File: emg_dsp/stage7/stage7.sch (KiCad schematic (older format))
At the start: 202 parts, among them U1 RS232_CON, U10 EN_VDD, U11 USBLC6, U12 ABM10XTAL-24, U13 BF527, U14 MIC5365, U15 AT25DF041-MHF, U16 ADSP_JTAG_CON, U17 LAN8710A, U18 74LCX541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

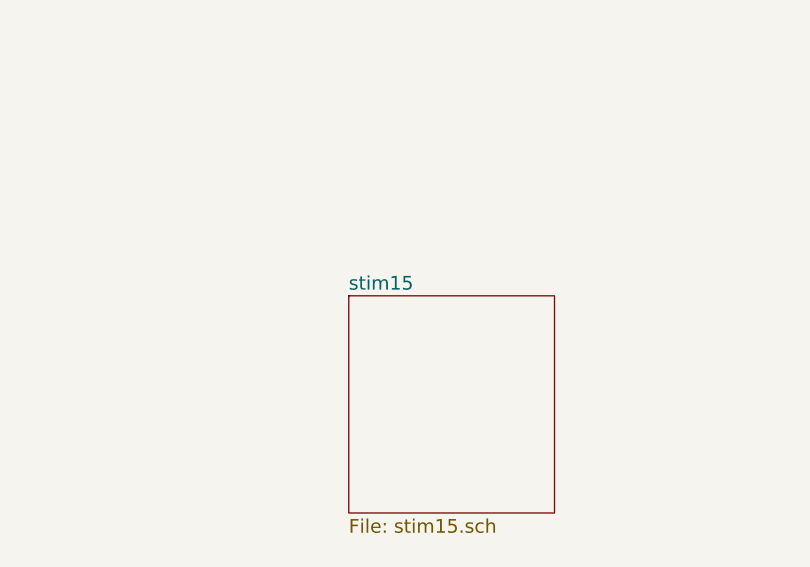
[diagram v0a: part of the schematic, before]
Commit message: placed modules in stim and wired, issues with shorting in stims
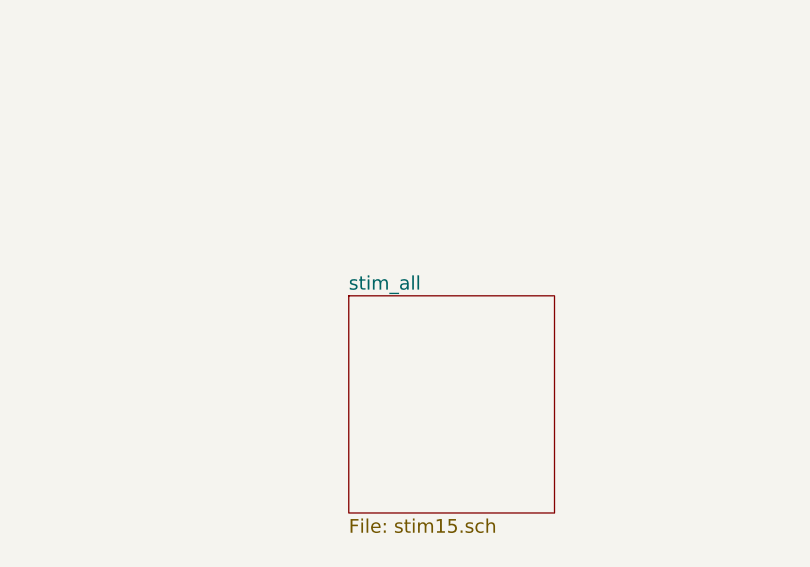
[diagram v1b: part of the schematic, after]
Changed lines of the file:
@@
-EESchema Schematic File Version 2  date Fri 21 Jan 2011 07:08:04 PM EST
+EESchema Schematic File Version 2  date Mon 24 Jan 2011 02:31:03 PM EST
 LIBS:power
 LIBS:device
@@
 Sheet 1 19
 Title "Stage 4 / Copyright 2010 Timothy L Hanson "
-Date "22 jan 2011"
+Date "24 jan 2011"
 Rev ""
 Comp "This design is free: redistribute or modify under the GPL v. 3 or later"
@@
 S 1450 4000 900  950
 U 4D2F608C
-F0 "stim15" 60
+F0 "stim_all" 60
 F1 "stim15.sch" 60
 $EndSheet

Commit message: more layout. getting there...
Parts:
- U15: value AT25DF041-MHF -> SST25VF040B
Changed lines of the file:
@@
-EESchema Schematic File Version 2  date Mon 24 Jan 2011 03:09:10 PM EST
+EESchema Schematic File Version 2  date Wed 26 Jan 2011 02:24:37 PM EST
 LIBS:power
 LIBS:device
@@
 Sheet 1 19
 Title "Stage 4 / Copyright 2010 Timothy L Hanson "
-Date "24 jan 2011"
+Date "26 jan 2011"
 Rev ""
 Comp "This design is free: redistribute or modify under the GPL v. 3 or later"
@@
 P 10100 700
 F 0 "U15" H 10150 450 60  0000 C CNN
-F 1 "AT25DF041-MHF" H 10150 1000 60  0000 C CNN
+F 1 "SST25VF040B" H 10150 1000 60  0000 C CNN
 F 2 "SOIC-8" H 10210 390 60  0000 C CNN
 	1    10100 700

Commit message: layout - stage 7 - got SDRAM and part of the Eth phy routed well. getting the rest of the components in their approx end positions.
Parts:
- removed C57, C58, C59: 15pf, 0402, symbol C
- added R? (x7): 130, 0402, symbol R
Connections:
- net GND: now also C51.1; no longer C51.2
- net MOSI: now also R?.2, R?.2, R?.2; no longer U24.5 (MOSI), U25.5 (MOSI), U26.5 (MOSI)
- net SCK: now also R?.1, R?.1, R?.1; no longer C52.2, C53.2, C54.2, U24.4 (SCK), U25.4 (SCK), U26.4 (SCK)
- new net: C52.2, R?.2, U24.4 (SCK)
- new net: R?.1, U24.5 (MOSI)
- new net: C51.2, R?.1, U18.4 (A3)
- new net: R?.2, U21.6 (SCK)
- new net: C53.2, R?.2, U25.4 (SCK)
- new net: R?.1, U25.5 (MOSI)
- new net: C54.2, R?.2, U26.4 (SCK)
- new net: R?.1, U26.5 (MOSI)
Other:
- moved on the sheet: C51

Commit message: getting there! about 70-80% done with individual routing.
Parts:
- gave numbers to parts that had none: 7

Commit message: layout of stage7 just about finished! need to check and make gerbers..
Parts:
- added TP38, TP39, TP40, TP41: TP, 2.9mm_hole, symbol TP
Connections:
- net GND: now also TP38.1, TP39.1, TP40.1, TP41.1
